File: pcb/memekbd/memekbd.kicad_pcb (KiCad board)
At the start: 2 copper layers, 3.6 x 3.1 mm, 194 parts, among them J1 MJ-4PP-9, J2 MJ-4PP-9, SW1 SW_Push, SW10 SW_Push, SW11 SW_Push, SW12 SW_Push, SW13 SW_Push, SW14 SW_Push, SW15 SW_Push, SW16 SW_Push, SW17 SW_Push, SW18 SW_Push, SW19 SW_Push, SW2 SW_Push, SW20 SW_Push, SW21 SW_Push, SW22 SW_Push, SW23 SW_Push, SW24 SW_Push, SW25 SW_Push, SW26 SW_Push, SW27 SW_Push, SW28 SW_Push, SW29 SW_Push, SW3 SW_Push, SW30 SW_Push, SW31 SW_Push, SW32 SW_Push, SW33 SW_Push, SW34 SW_Push, SW35 SW_Push, SW36 SW_Push, SW37 SW_Push, SW38 SW_Push, SW39 SW_Push, SW4 SW_Push, SW40 SW_Push, SW41 SW_Push, SW42 SW_Push, SW43 SW_Push, SW44 SW_Push, SW45 SW_Push, SW46 SW_Push, SW47 SW_Push, SW48 SW_Push, SW5 SW_Push, SW6 SW_Push, SW7 SW_Push, SW8 SW_Push, SW9 SW_Push, U1 ProMicro, U2 ProMicro

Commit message: More pcb layout.
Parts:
- LED1, LED10, LED11, LED12, LED13, LED14, LED15, LED16, LED17, LED18, LED19, LED2, LED20, LED21, LED22, LED23, LED24, LED25, LED26, LED27, LED28, LED29, LED3, LED30, LED31, LED32, LED33, LED34, LED35, LED36, LED37, LED38, LED39, LED4, LED40, LED41, LED42, LED43, LED44, LED45, LED46, LED5, LED6, LED7, LED8, LED9: moved to B.Cu
- moved U2 4.00 mm to (130.5, 28.0)
- moved LED4 1.00 mm to (-19.0, 71.5)
- moved LED6 1.00 mm to (0.00, 14.5)
- moved LED9 0.78 mm to (0.00, 71.5)
- moved LED15 0.78 mm to (38.0, -4.50)
- moved LED1 0.71 mm to (-19.0, 14.5)
- moved LED12 0.71 mm to (19.0, 33.5)
- moved LED16 0.71 mm to (38.0, 14.5)
- moved LED17 0.71 mm to (38.0, 33.5)
- moved LED20 0.71 mm to (57.0, 14.5)
- moved LED21 0.71 mm to (57.0, 33.5)
- moved LED22 0.71 mm to (57.0, 52.5)
- moved LED27 0.71 mm to (154.5, 71.5)
- moved LED29 0.71 mm to (173.5, 14.5)
- moved LED31 0.71 mm to (173.5, 52.5)
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
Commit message: Finish layout
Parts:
- moved D24 1.58 mm to (158.5, 27.5)
- moved D30 1.58 mm to (177.5, 46.5)
- moved D34 1.58 mm to (196.5, 27.5)
- moved D35 1.58 mm to (196.5, 46.5)
- moved D39 1.58 mm to (215.5, 27.5)
- moved D41 1.58 mm to (215.5, 65.5)
- moved D15 1.12 mm to (42.0, 8.50)
- moved D17 1.12 mm to (42.0, 46.5)
- moved D19 1.12 mm to (42.0, 84.5)
- moved D20 1.12 mm to (61.0, 27.5)
- moved D21 1.12 mm to (61.0, 46.5)
- moved D22 1.12 mm to (61.0, 65.5)
- moved D25 1.12 mm to (158.5, 46.5)
- moved D28 1.12 mm to (177.5, 8.50)
- moved D29 1.12 mm to (177.5, 27.5)
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
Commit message: Stagger
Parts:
- moved J2 59.0 mm to (179.2, 22.8)
- moved R3 59.0 mm to (188.8, 32.2)
- moved R4 59.0 mm to (188.8, 28.2)
- moved SW48 59.0 mm to (181.8, 36.8)
- moved U2 59.0 mm to (184.2, 3.75)
- moved C33 56.8 mm to (249.5, -22.0)
- moved C34 56.8 mm to (249.5, -3.00)
- moved C35 56.8 mm to (249.0, 16.5)
- moved C36 56.8 mm to (249.0, 35.0)
- moved D33 56.8 mm to (251.5, -5.50)
- moved D34 56.8 mm to (251.5, 13.5)
- moved D35 56.8 mm to (251.5, 32.5)
- moved D36 56.8 mm to (251.5, 51.5)
- moved LED33 56.8 mm to (247.5, -18.5)
- moved LED34 56.8 mm to (247.5, 0.50)
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
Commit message: Thumb position
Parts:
- moved C23 67.2 mm to (143.2, 124.2)
- moved D23 67.2 mm to (145.2, 140.8)
- moved LED23 67.2 mm to (141.2, 127.8)
- moved SW23 67.2 mm to (141.2, 132.2)
- moved C19 48.3 mm to (114.2, 108.2)
- moved D19 48.3 mm to (116.2, 124.8)
- moved LED19 48.3 mm to (112.2, 111.8)
- moved SW19 48.3 mm to (112.2, 116.2)
- moved C14 32.8 mm to (85.2, 96.2)
- moved D14 32.8 mm to (87.2, 112.8)
- moved LED14 32.8 mm to (83.2, 99.8)
- moved SW14 32.8 mm to (83.2, 104.2)
- moved C9 21.3 mm to (55.8, 88.2)
- moved D9 21.3 mm to (58.2, 104.8)
- moved LED9 21.3 mm to (54.2, 91.8)
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
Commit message: Fix up thumb positions.
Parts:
- moved C1 63.6 mm to (30.8, 53.5)
- moved C10 63.6 mm to (68.2, 20.5)
- moved C11 63.6 mm to (68.2, 40.0)
- moved C12 63.6 mm to (68.2, 58.5)
- moved C13 63.6 mm to (68.2, 78.0)
- moved C15 63.6 mm to (86.8, 27.5)
- moved C16 63.6 mm to (86.8, 47.0)
- moved C17 63.6 mm to (86.8, 65.5)
- moved C18 63.6 mm to (87.2, 84.5)
- moved C2 63.6 mm to (30.8, 72.5)
- moved C20 63.6 mm to (106.8, 46.5)
- moved C21 63.6 mm to (106.2, 66.0)
- moved C22 63.6 mm to (105.8, 84.5)
- moved C24 63.6 mm to (276.8, 46.5)
- moved C25 63.6 mm to (276.8, 65.5)
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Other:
- board size 3.6 x 3.1 mm -> 4.7 x 4.7 mm

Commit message: Finish key positions.
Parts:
- moved SW27 21.9 mm to (239.0, 136.5), turned to 225 degrees
- moved D27 21.5 mm to (247.9, 139.7), turned to 225 degrees
- moved LED27 21.5 mm to (235.8, 133.3), turned to 45 degrees
- moved C27 19.9 mm to (234.8, 129.4), turned to 225 degrees
- moved U2 18.2 mm to (255.5, 63.2)
- moved C46 18.0 mm to (322.5, 110.8), turned to 150 degrees
- moved U1 16.7 mm to (123.0, 63.2)
- moved LED46 16.5 mm to (319.0, 112.9), turned to 330 degrees
- moved J2 16.4 mm to (246.5, 81.5)
- moved R4 15.9 mm to (255.5, 86.5)
- moved R3 15.4 mm to (255.5, 90.0)
- moved J1 14.5 mm to (132.0, 81.5)
- moved SW48 14.4 mm to (248.5, 93.5)
- moved C42 14.4 mm to (300.0, 107.2), turned to 165 degrees
- moved SW46 14.4 mm to (316.8, 116.8), turned to 150 degrees
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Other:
- outline, holes or cut-outs redrawn

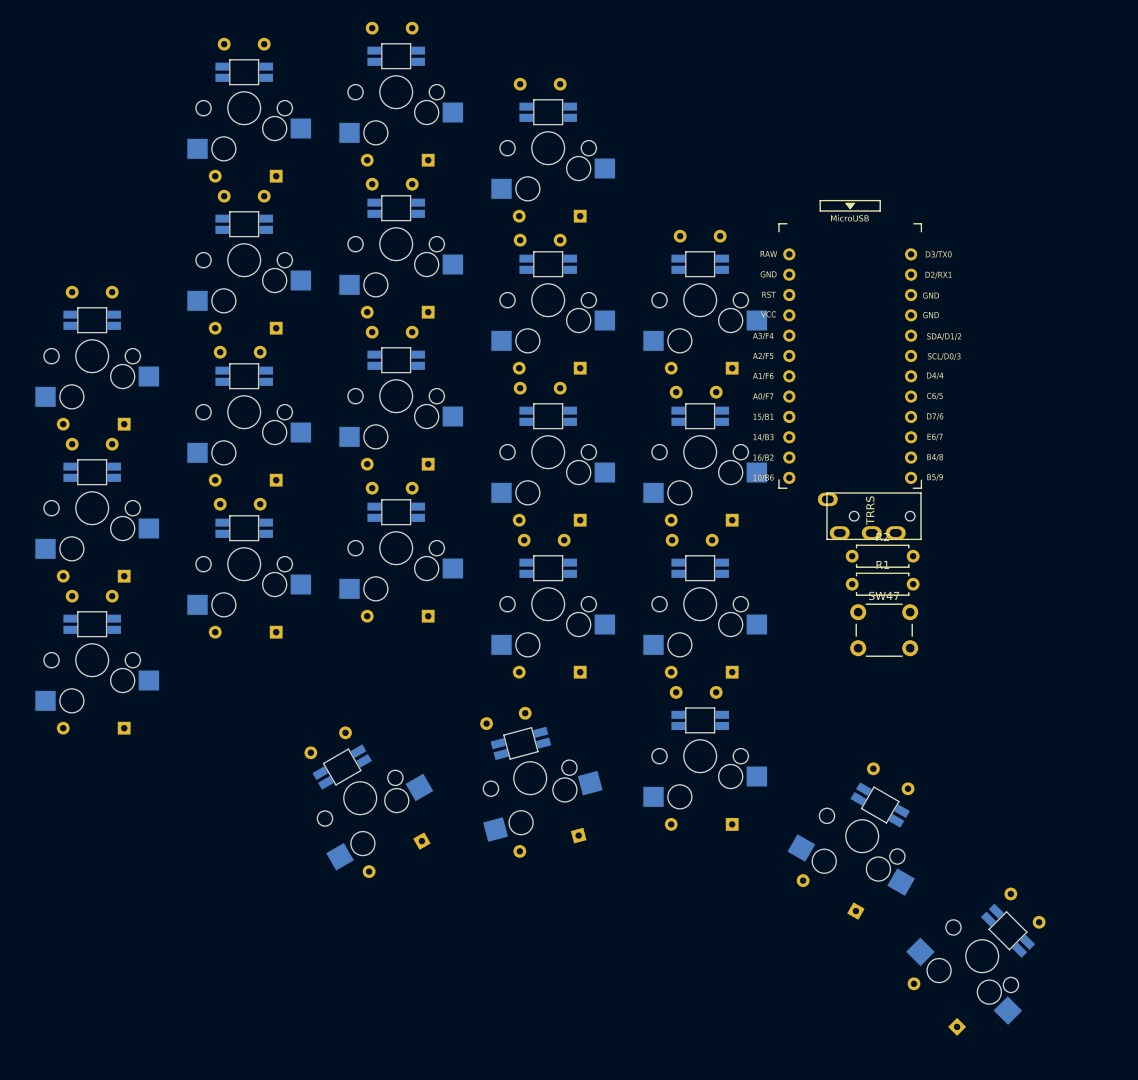
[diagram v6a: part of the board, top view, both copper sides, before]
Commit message: Start edge cuts.
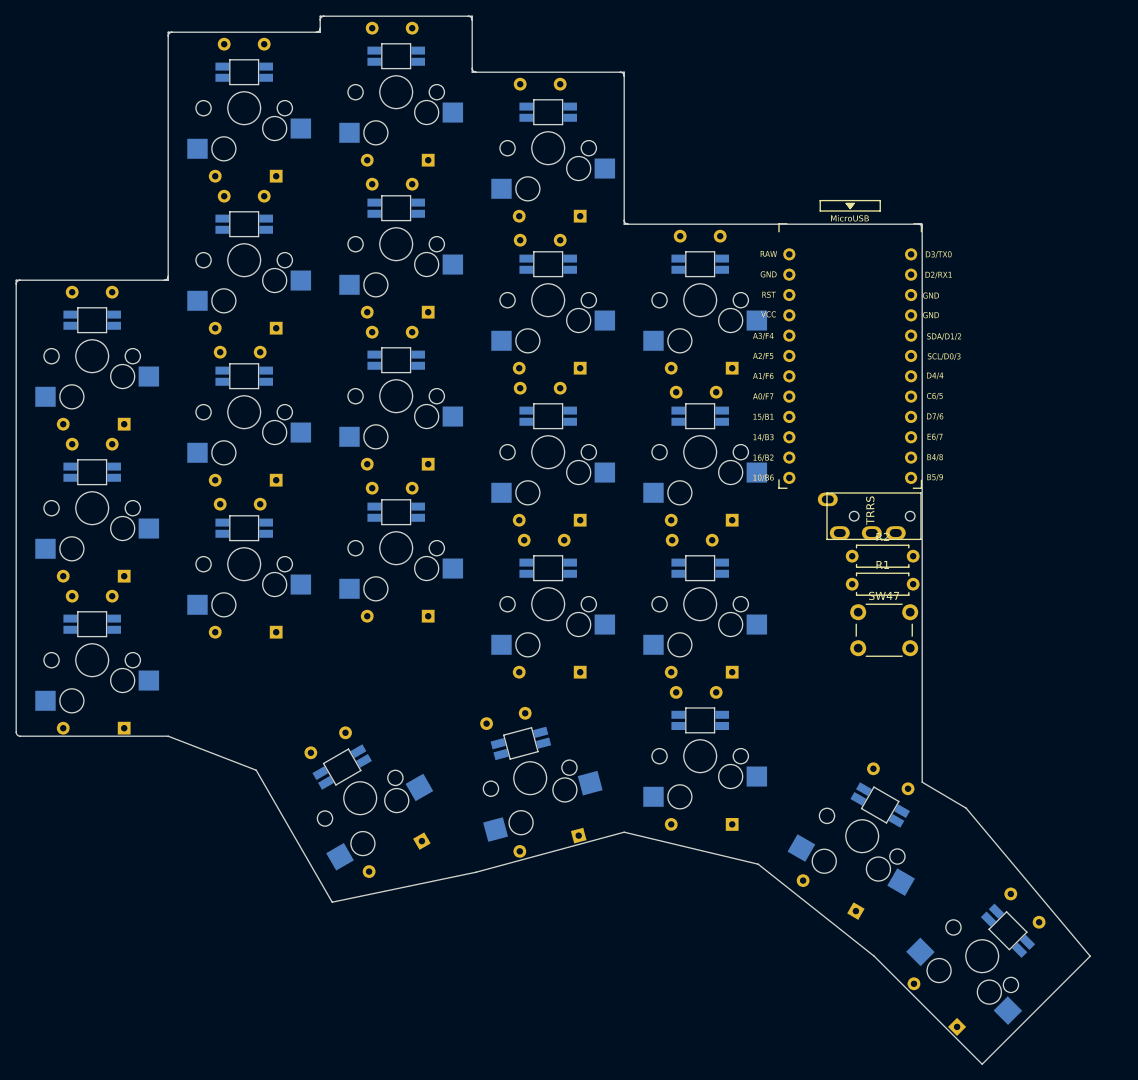
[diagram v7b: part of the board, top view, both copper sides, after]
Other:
- board size 4.7 x 4.7 mm -> 134.2 x 131 mm
- net class Power added: clearance 0.2, trace_width 0.5, via_dia 0.8, via_drill 0.4
- rule pad_to_mask_clearance: 0 -> 0.05
- rule via_min_size: 0.4 -> 0.6
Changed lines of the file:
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@@
   (general
     (thickness 1.6)
-    (drawings 0)
+    (drawings 34)
     (tracks 0)
     (zones 0)
@@
     (via_size 0.8)
     (via_drill 0.4)
-    (via_min_size 0.4)
+    (via_min_size 0.6)
     (via_min_drill 0.3)
     (uvia_size 0.3)
@@
     (pad_size 1.524 1.524)
     (pad_drill 0.762)
-    (pad_to_mask_clearance 0)
+    (pad_to_mask_clearance 0.05)
     (aux_axis_origin 0 0)
     (visible_elements FFFFFF7F)
@@
     (uvia_dia 0.3)
     (uvia_drill 0.1)
-    (add_net +5V)
     (add_net /lLED)
     (add_net /lRST)
@@
     (add_net /rrow3)
     (add_net /rrow4)
-    (add_net GND)
     (add_net "Net-(D1-Pad2)")
     (add_net "Net-(D10-Pad2)")
@@
     (add_net "Net-(U2-Pad24)")
   )
+  (net_class Power ""
+    (clearance 0.2)
+    (trace_width 0.5)
+    (via_dia 0.8)
+    (via_drill 0.4)
+    (uvia_dia 0.3)
+    (uvia_drill 0.1)
+    (add_net +5V)
+    (add_net GND)
+  )
   (module kbd:MJ-4PP-9_1side (layer F.Cu)
     (at 246.5 81.5 90)
@@
     )
   )
+  (gr_arc (start 131.5 45.5) (end 132 45.5) (angle -90) (layer Edge.Cuts) (width 0.05))
+  (gr_arc (start 95.25 44.5) (end 94.75 44.5) (angle -90) (layer Edge.Cuts) (width 0.05))
+  (gr_arc (start 94.25 26.5) (end 94.75 26.5) (angle -90) (layer Edge.Cuts) (width 0.05))
+  (gr_arc (start 76.25 25.5) (end 75.75 25.5) (angle -90) (layer Edge.Cuts) (width 0.05))
+  (gr_arc (start 75.25 19.5) (end 75.75 19.5) (angle -90) (layer Edge.Cuts) (width 0.05))
+  (gr_arc (start 57.25 19.5) (end 57.25 19) (angle -90) (layer Edge.Cuts) (width 0.05))
+  (gr_arc (start 56.25 20.5) (end 56.25 21) (angle -90) (layer Edge.Cuts) (width 0.05))
+  (gr_arc (start 38.25 21.5) (end 38.25 21) (angle -90) (layer Edge.Cuts) (width 0.05))
+  (gr_arc (start 37.25 51.5) (end 37.25 52) (angle -90) (layer Edge.Cuts) (width 0.05))
+  (gr_arc (start 19.25 52.5) (end 19.25 52) (angle -90) (layer Edge.Cuts) (width 0.05))
+  (gr_arc (start 19.25 108.5) (end 18.75 108.5) (angle -90) (layer Edge.Cuts) (width 0.05))
+  (gr_line (start 137.5 118) (end 153 136.5) (layer Edge.Cuts) (width 0.05))
+  (gr_line (start 37.75 109) (end 19.25 109) (layer Edge.Cuts) (width 0.05))
+  (gr_line (start 48.75 113.25) (end 37.75 109) (layer Edge.Cuts) (width 0.05))
+  (gr_line (start 58.25 129.75) (end 48.75 113.25) (layer Edge.Cuts) (width 0.05))
+  (gr_line (start 76.25 126) (end 58.25 129.75) (layer Edge.Cuts) (width 0.05))
+  (gr_line (start 94.75 121) (end 76.25 126) (layer Edge.Cuts) (width 0.05))
+  (gr_line (start 111.5 125) (end 94.75 121) (layer Edge.Cuts) (width 0.05))
+  (gr_line (start 126 136.5) (end 111.5 125) (layer Edge.Cuts) (width 0.05))
+  (gr_line (start 139.5 150) (end 126 136.5) (layer Edge.Cuts) (width 0.05))
+  (gr_line (start 153 136.5) (end 139.5 150) (layer Edge.Cuts) (width 0.05))
+  (gr_line (start 132 114.75) (end 137.5 118) (layer Edge.Cuts) (width 0.05))
+  (gr_line (start 132 45) (end 132 114.75) (layer Edge.Cuts) (width 0.05))
+  (gr_line (start 131.75 45) (end 132 45) (layer Edge.Cuts) (width 0.05))
+  (gr_line (start 94.75 45) (end 131.75 45) (layer Edge.Cuts) (width 0.05))
+  (gr_line (start 94.75 26) (end 94.75 45) (layer Edge.Cuts) (width 0.05))
+  (gr_line (start 75.75 26) (end 94.75 26) (layer Edge.Cuts) (width 0.05))
+  (gr_line (start 75.75 19) (end 75.75 26) (layer Edge.Cuts) (width 0.05))
+  (gr_line (start 56.75 19) (end 75.75 19) (layer Edge.Cuts) (width 0.05))
+  (gr_line (start 56.75 21) (end 56.75 19) (layer Edge.Cuts) (width 0.05))
+  (gr_line (start 37.75 21) (end 56.75 21) (layer Edge.Cuts) (width 0.05))
+  (gr_line (start 37.75 52) (end 37.75 21) (layer Edge.Cuts) (width 0.05))
+  (gr_line (start 18.75 52) (end 37.75 52) (layer Edge.Cuts) (width 0.05))
+  (gr_line (start 18.75 108.5) (end 18.75 52) (layer Edge.Cuts) (width 0.05))
 )

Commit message: Rounded corners.
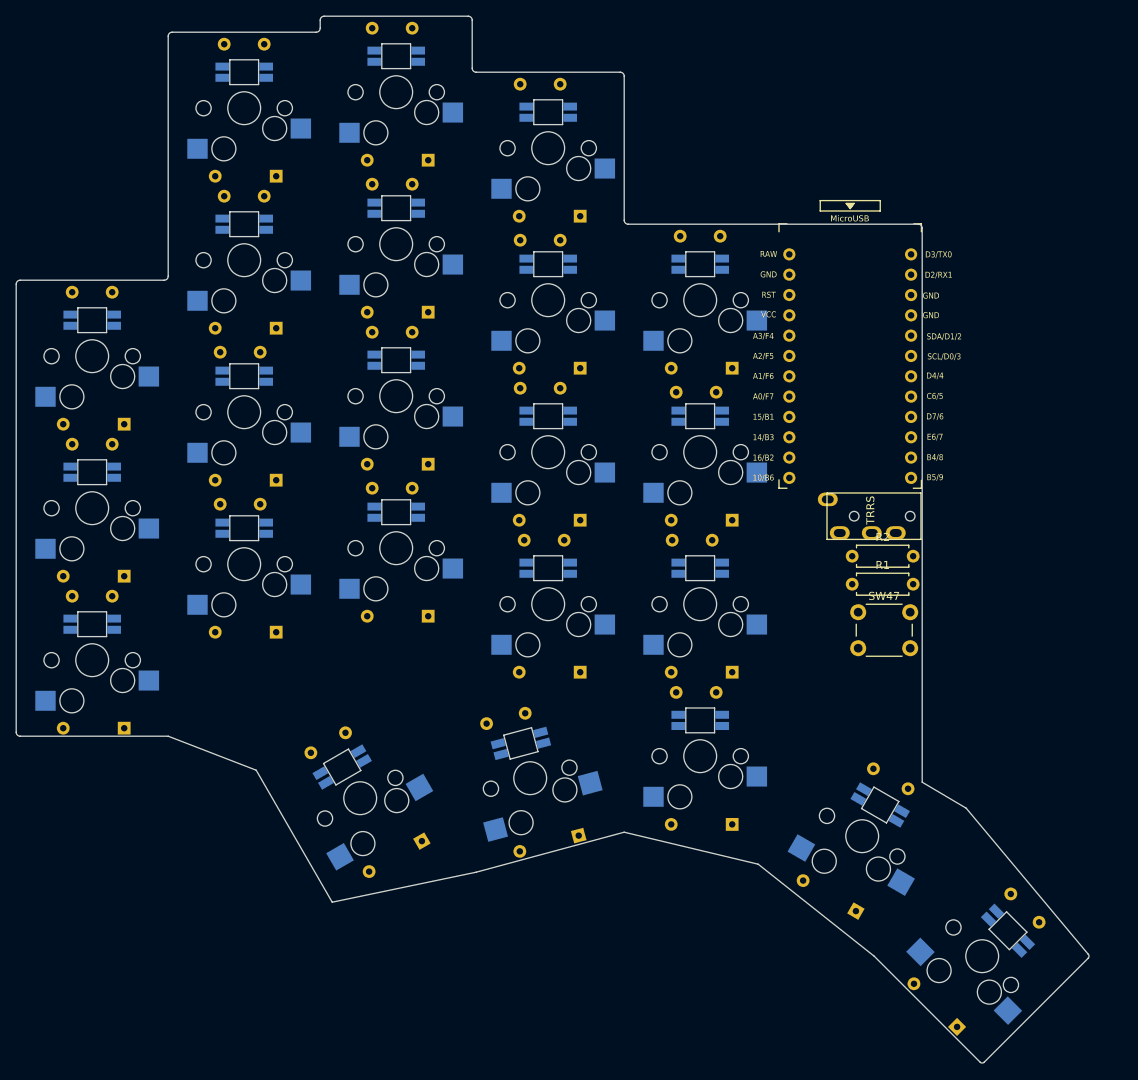
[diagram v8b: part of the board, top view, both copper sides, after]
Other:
- board size 134.2 x 131 mm -> 134.1 x 130.9 mm
